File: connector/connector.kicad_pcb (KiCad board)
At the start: 2 copper layers, 18.7 x 4.8 mm, 10 parts, among them P11 CONN_1, P12 CONN_1, P13 CONN_1, P14 CONN_1, P15 CONN_1, P21 CONN_1, P22 CONN_1, P23 CONN_1, P24 CONN_1, P25 CONN_1

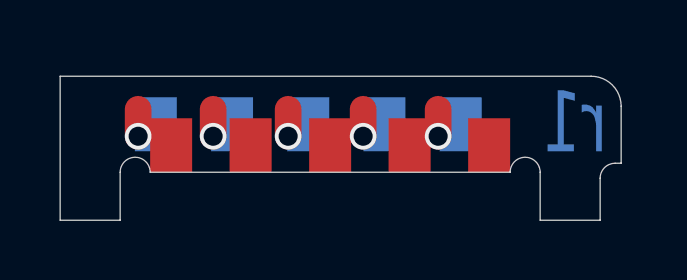
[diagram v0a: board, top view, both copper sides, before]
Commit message: Remove old tracks.
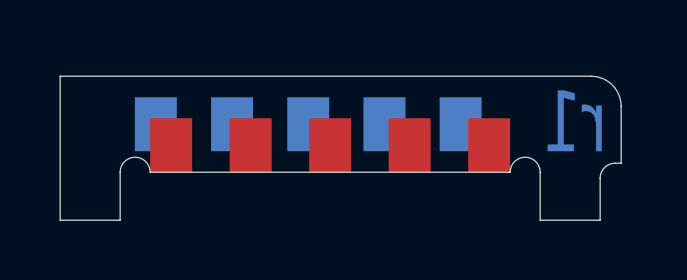
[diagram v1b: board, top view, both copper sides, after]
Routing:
- net N-000005: track 1.82 -> 0.00 mm, vias 1 -> 0
- net N-000004: track 1.78 -> 0.00 mm, vias 1 -> 0
- net N-000003: track 1.74 -> 0.00 mm, vias 1 -> 0
- net N-000002: track 1.70 -> 0.00 mm, vias 1 -> 0
- net N-000001: track 1.66 -> 0.00 mm, vias 1 -> 0
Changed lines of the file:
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@@
   (general
     (links 5)
-    (no_connects 0)
+    (no_connects 5)
     (area 108.257145 78.7 181.149997 104.3542)
     (thickness 1.6002)
     (drawings 21)
-    (tracks 20)
+    (tracks 0)
     (zones 0)
     (modules 10)
@@
   (gr_line (start 138.4 102.4) (end 140.4 102.4) (angle 90) (layer Edge.Cuts) (width 0.01))
   (gr_line (start 140.4 102.4) (end 140.4 100.8) (angle 90) (layer Edge.Cuts) (width 0.01))
-  (via (at 141 99.6) (size 0.889) (drill 0.635) (layers Front Back) (net 1))
-  (segment (start 141 99.6) (end 141.19 99.6) (width 0.889) (layer Back) (net 1))
-  (segment (start 141.19 99.6) (end 141.59 99.2) (width 0.889) (layer Back) (net 1))
-  (segment (start 141 98.7) (end 141 99.6) (width 0.889) (layer Front) (net 1))
-  (via (at 143.5 99.6) (size 0.889) (drill 0.635) (layers Front Back) (net 2))
-  (segment (start 143.5 99.6) (end 143.73 99.6) (width 0.889) (layer Back) (net 2))
-  (segment (start 143.73 99.6) (end 144.13 99.2) (width 0.889) (layer Back) (net 2))
-  (segment (start 143.5 98.7) (end 143.5 99.6) (width 0.889) (layer Front) (net 2))
-  (via (at 146 99.6) (size 0.889) (drill 0.635) (layers Front Back) (net 3))
-  (segment (start 146 99.6) (end 146.27 99.6) (width 0.889) (layer Back) (net 3))
-  (segment (start 146.27 99.6) (end 146.67 99.2) (width 0.889) (layer Back) (net 3))
-  (segment (start 146 98.7) (end 146 99.6) (width 0.889) (layer Front) (net 3))
-  (via (at 148.5 99.6) (size 0.889) (drill 0.635) (layers Front Back) (net 4))
-  (segment (start 148.5 99.6) (end 148.81 99.6) (width 0.889) (layer Back) (net 4))
-  (segment (start 148.81 99.6) (end 149.21 99.2) (width 0.889) (layer Back) (net 4))
-  (segment (start 148.5 98.7) (end 148.5 99.6) (width 0.889) (layer Front) (net 4))
-  (via (at 151 99.6) (size 0.889) (drill 0.635) (layers Front Back) (net 5))
-  (segment (start 151 99.6) (end 151.35 99.6) (width 0.889) (layer Back) (net 5))
-  (segment (start 151.35 99.6) (end 151.75 99.2) (width 0.889) (layer Back) (net 5))
-  (segment (start 151 98.7) (end 151 99.6) (width 0.889) (layer Front) (net 5))
 )

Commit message: Update revision number.
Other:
- board text added: "r2"
- board text removed: "r1"
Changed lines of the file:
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@@
     (arrow2b (pts (xy 138.4 95.6) (xy 139.526504 95.013579)))
   )
-  (gr_text r1 (at 155.5496 99.1616) (layer B.Mask)
+  (gr_text r2 (at 155.5496 99.1616) (layer B.Mask)
     (effects (font (size 2.032 1.524) (thickness 0.3048)) (justify mirror))
   )
-  (gr_text r1 (at 155.5496 99.1616) (layer Back)
+  (gr_text r2 (at 155.5496 99.1616) (layer Back)
     (effects (font (size 2.032 1.524) (thickness 0.3048)) (justify mirror))
   )

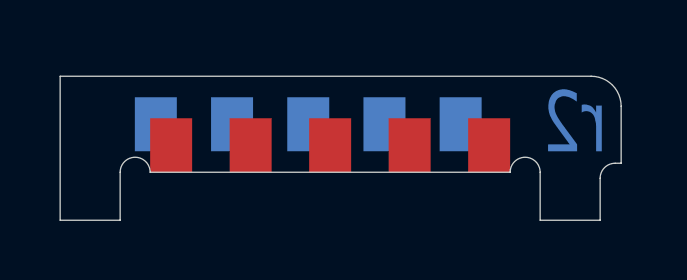
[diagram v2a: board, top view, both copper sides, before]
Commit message: Precisely position vias.
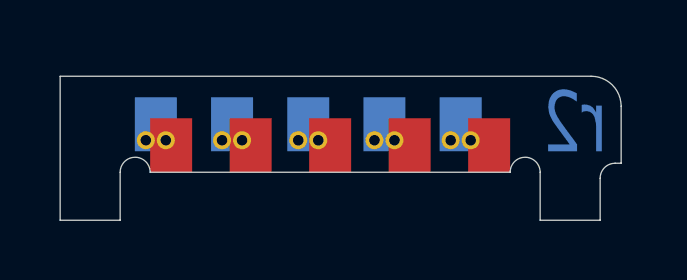
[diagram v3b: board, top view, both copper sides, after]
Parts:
- added ?: VAL**, UGL:via_24_14mil, F.Cu at (141.9, 99.8)
- added via_24_14mil: VAL**, UGL:via_24_14mil, F.Cu at (152.0, 99.7)
- added via_24_14mil: VAL**, UGL:via_24_14mil, F.Cu at (151.4, 99.7)
- added via_24_14mil: VAL**, UGL:via_24_14mil, F.Cu at (148.9, 99.7)
- added via_24_14mil: VAL**, UGL:via_24_14mil, F.Cu at (149.6, 99.7)
- added via_24_14mil: VAL**, UGL:via_24_14mil, F.Cu at (147.0, 99.7)
- added via_24_14mil: VAL**, UGL:via_24_14mil, F.Cu at (146.3, 99.7)
- added via_24_14mil: VAL**, UGL:via_24_14mil, F.Cu at (143.8, 99.7)
- added via_24_14mil: VAL**, UGL:via_24_14mil, F.Cu at (141.3, 99.8)
- added via_24_14mil: VAL**, UGL:via_24_14mil, F.Cu at (144.4, 99.7)
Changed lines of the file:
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@@
 (kicad_pcb (version 4) (host pcbnew "(2014-jul-16 BZR unknown)-product")
   (general
-    (links 5)
-    (no_connects 5)
+    (links 15)
+    (no_connects 0)
     (area 108.257145 78.7 181.149997 104.3542)
     (thickness 1.6002)
@@
     (tracks 0)
     (zones 0)
-    (modules 10)
+    (modules 20)
     (nets 6)
   )
@@
     (mod_text_size 1.524 1.524)
     (mod_text_width 0.3048)
-    (pad_size 1.4 1.8)
-    (pad_drill 0)
+    (pad_size 0.6 0.6)
+    (pad_drill 0.35)
     (pad_to_mask_clearance 0.1016)
     (aux_axis_origin 0 0)
-    (visible_elements FFFFFF7F)
+    (visible_elements FFFFFD7F)
     (pcbplotparams
       (layerselection 0x00030_80000001)
@@
     (add_net N-000005)
   )
+  (module UGL:via_24_14mil (layer Front)
+    (at 152.0444 99.73564)
+    (fp_text reference via_24_14mil (at 0 -1.8) (layer F.SilkS) hide
+      (effects (font (size 1 1) (thickness 0.15)))
+    )
+    (fp_text value VAL** (at 0 1.9) (layer F.SilkS) hide
+      (effects (font (size 1 1) (thickness 0.15)))
+    )
+    (pad "" thru_hole circle (at 0.038933 -0.002307) (size 0.6 0.6) (drill 0.35) (layers *.Cu *.Mask F.SilkS)
+      (net 5 N-000005) (solder_mask_margin -1) (clearance 0.01))
+  )
+  (module UGL:via_24_14mil (layer Front)
+    (at 151.37384 99.73564)
+    (fp_text reference via_24_14mil (at 0 -1.8) (layer F.SilkS) hide
+      (effects (font (size 1 1) (thickness 0.15)))
+    )
+    (fp_text value VAL** (at 0 1.9) (layer F.SilkS) hide
+      (effects (font (size 1 1) (thickness 0.15)))
+    )
+    (pad "" thru_hole circle (at 0.042827 -0.002307) (size 0.6 0.6) (drill 0.35) (layers *.Cu *.Mask F.SilkS)
+      (net 5 N-000005) (solder_mask_margin -1) (clearance 0.01))
+  )
+  (module UGL:via_24_14mil (layer Front)
+    (at 148.87956 99.74072)
+    (fp_text reference via_24_14mil (at 0 -1.8) (layer F.SilkS) hide
+      (effects (font (size 1 1) (thickness 0.15)))
+    )
+    (fp_text value VAL** (at 0 1.9) (layer F.SilkS) hide
+      (effects (font (size 1 1) (thickness 0.15)))
+    )
+    (pad "" thru_hole circle (at -0.002893 -0.007387) (size 0.6 0.6) (drill 0.35) (layers *.Cu *.Mask F.SilkS)
+      (net 4 N-000004) (solder_mask_margin -1) (clearance 0.01))
+  )
+  (module UGL:via_24_14mil (layer Front)
+    (at 149.55012 99.74072)
+    (fp_text reference via_24_14mil (at 0 -1.8) (layer F.SilkS) hide
+      (effects (font (size 1 1) (thickness 0.15)))
+    )
+    (fp_text value VAL** (at 0 1.9) (layer F.SilkS) hide
+      (effects (font (size 1 1) (thickness 0.15)))
+    )
+    (pad "" thru_hole circle (at -0.006787 -0.007387) (size 0.6 0.6) (drill 0.35) (layers *.Cu *.Mask F.SilkS)
+      (net 4 N-000004) (solder_mask_margin -1) (clearance 0.01))
+  )
+  (module UGL:via_24_14mil (layer Front)
+    (at 146.99996 99.7204)
+    (fp_text reference via_24_14mil (at 0 -1.8) (layer F.SilkS) hide
+      (effects (font (size 1 1) (thickness 0.15)))
+    )
+    (fp_text value VAL** (at 0 1.9) (layer F.SilkS) hide
+      (effects (font (size 1 1) (thickness 0.15)))
+    )
+    (pad "" thru_hole circle (at 0.003373 0.012933) (size 0.6 0.6) (drill 0.35) (layers *.Cu *.Mask F.SilkS)
+      (net 3 N-000003) (solder_mask_margin -1) (clearance 0.01))
+  )
+  (module UGL:via_24_14mil (layer Front)
+    (at 146.3294 99.7204)
+    (fp_text reference via_24_14mil (at 0 -1.8) (layer F.SilkS) hide
+      (effects (font (size 1 1) (thickness 0.15)))
+    )
+    (fp_text value VAL** (at 0 1.9) (layer F.SilkS) hide
+      (effects (font (size 1 1) (thickness 0.15)))
+    )
+    (pad "" thru_hole circle (at 0.007267 0.012933) (size 0.6 0.6) (drill 0.35) (layers *.Cu *.Mask F.SilkS)
+      (net 3 N-000003) (solder_mask_margin -1) (clearance 0.01))
+  )
+  (module UGL:via_24_14mil (layer Front)
+    (at 143.77924 99.73564)
+    (fp_text reference via_24_14mil (at 0 -1.8) (layer F.SilkS) hide
+      (effects (font (size 1 1) (thickness 0.15)))
+    )
+    (fp_text value VAL** (at 0 1.9) (layer F.SilkS) hide
+      (effects (font (size 1 1) (thickness 0.15)))
+    )
+    (pad "" thru_hole circle (at 0.017427 -0.002307) (size 0.6 0.6) (drill 0.35) (layers *.Cu *.Mask F.SilkS)
+      (net 2 N-000002) (solder_mask_margin -1) (clearance 0.01))
+  )
   (module vertical_pcb_pad (layer Back)
     (at 151.75 99.2)
@@
       (net 2 N-000002))
   )
+  (module UGL:via_24_14mil (layer Front)
+    (at 141.93012 99.75088)
+    (fp_text reference "" (at 0 -1.8) (layer F.SilkS) hide
+      (effects (font (size 1 1) (thickness 0.15)))
+    )
+    (fp_text value VAL** (at 0 1.9) (layer F.SilkS) hide
+      (effects (font (size 1 1) (thickness 0.15)))
+    )
+    (pad "" thru_hole circle (at -0.006787 -0.017547) (size 0.6 0.6) (drill 0.35) (layers *.Cu *.Mask F.SilkS)
+      (net 1 N-000001) (solder_mask_margin -1) (clearance 0.01))
+  )
+  (module UGL:via_24_14mil (layer Front)
+    (at 141.25956 99.76612)
+    (fp_text reference via_24_14mil (at 0 -1.8) (layer F.SilkS) hide
+      (effects (font (size 1 1) (thickness 0.15)))
+    )
+    (fp_text value VAL** (at 0 1.9) (layer F.SilkS) hide
+      (effects (font (size 1 1) (thickness 0.15)))
+    )
+    (pad "" thru_hole circle (at -0.002893 -0.032787) (size 0.6 0.6) (drill 0.35) (layers *.Cu *.Mask F.SilkS)
+      (net 1 N-000001) (solder_mask_margin -1) (clearance 0.01))
+  )
+  (module UGL:via_24_14mil (layer Front)
+    (at 144.4498 99.73564)
+    (fp_text reference via_24_14mil (at 0 -1.8) (layer F.SilkS) hide
+      (effects (font (size 1 1) (thickness 0.15)))
+    )
+    (fp_text value VAL** (at 0 1.9) (layer F.SilkS) hide
+      (effects (font (size 1 1) (thickness 0.15)))
+    )
+    (pad "" thru_hole circle (at 0.013533 -0.002307) (size 0.6 0.6) (drill 0.35) (layers *.Cu *.Mask F.SilkS)
+      (net 2 N-000002) (solder_mask_margin -1) (clearance 0.01))
+  )
   (gr_text "4.8 mm = 0.188976 in" (at 121.8 100) (layer Cmts.User)

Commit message: Connect the front and back pads.
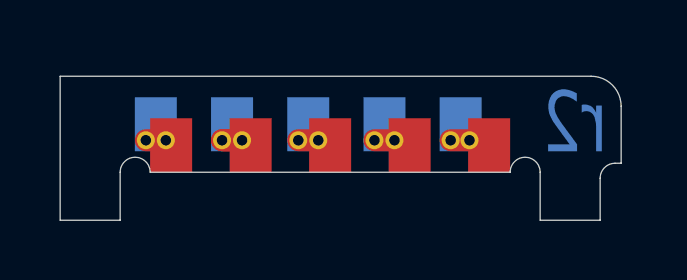
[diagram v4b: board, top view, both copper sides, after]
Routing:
- net N-000002: track 0.00 -> 2.36 mm
- net N-000001: track 0.00 -> 2.23 mm
- net N-000005: track 0.00 -> 2.01 mm
- net N-000004: track 0.00 -> 1.91 mm
- net N-000003: track 0.00 -> 1.80 mm
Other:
- rule trace_min: 0.889 -> 0.6
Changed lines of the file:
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@@
     (thickness 1.6002)
     (drawings 21)
-    (tracks 0)
+    (tracks 22)
     (zones 0)
     (modules 20)
@@
   )
   (setup
-    (last_trace_width 0.889)
-    (user_trace_width 0.889)
+    (last_trace_width 0.733)
+    (user_trace_width 0.733)
     (trace_clearance 0.635)
     (zone_clearance 0.508)
     (zone_45_only no)
-    (trace_min 0.889)
+    (trace_min 0.6)
     (segment_width 0.381)
     (edge_width 0.01016)
@@
     (mod_text_size 1.524 1.524)
     (mod_text_width 0.3048)
-    (pad_size 0.6 0.6)
-    (pad_drill 0.35)
+    (pad_size 1.4 1.8)
+    (pad_drill 0)
     (pad_to_mask_clearance 0.1016)
     (aux_axis_origin 0 0)
-    (visible_elements FFFFFD7F)
+    (visible_elements FFFFFF7F)
     (pcbplotparams
       (layerselection 0x00030_80000001)
@@
       (effects (font (size 1 1) (thickness 0.15)))
     )
-    (pad "" thru_hole circle (at 0.038933 -0.002307) (size 0.6 0.6) (drill 0.35) (layers *.Cu *.Mask F.SilkS)
+    (pad "" thru_hole circle (at 0 -0.002307) (size 0.6 0.6) (drill 0.35) (layers *.Cu *.Mask F.SilkS)
       (net 5 N-000005) (solder_mask_margin -1) (clearance 0.01))
   )
@@
   (gr_line (start 138.4 102.4) (end 140.4 102.4) (angle 90) (layer Edge.Cuts) (width 0.01))
   (gr_line (start 140.4 102.4) (end 140.4 100.8) (angle 90) (layer Edge.Cuts) (width 0.01))
+  (segment (start 141.93012 99.74072) (end 141.59 99.2) (width 0.733) (layer Back) (net 1))
+  (segment (start 141.59 99.2) (end 141.93012 99.54012) (width 0.733) (layer Back) (net 1))
+  (segment (start 141.93012 99.54012) (end 141.93012 99.74072) (width 0.733) (layer Back) (net 1))
+  (segment (start 141.256667 99.733333) (end 141.933333 99.733333) (width 0.733) (layer Front) (net 1))
+  (segment (start 141.933333 99.733333) (end 142.1 99.9) (width 0.733) (layer Front) (net 1))
+  (segment (start 144.13 99.2) (end 144.13 99.4) (width 0.733) (layer Back) (net 2))
+  (segment (start 144.583333 99.733333) (end 143.796667 99.733333) (width 0.733) (layer Front) (net 2))
+  (segment (start 144.75 99.9) (end 144.583333 99.733333) (width 0.733) (layer Front) (net 2))
+  (segment (start 144.13 99.4) (end 143.796667 99.733333) (width 0.733) (layer Back) (net 2))
+  (segment (start 143.796667 99.733333) (end 144.463333 99.733333) (width 0.733) (layer Front) (net 2))
+  (segment (start 146.67 99.2) (end 147.003333 99.533333) (width 0.733) (layer Back) (net 3))
+  (segment (start 147.003333 99.533333) (end 147.003333 99.733333) (width 0.733) (layer Back) (net 3))
+  (segment (start 147.4 99.9) (end 147.233333 99.733333) (width 0.733) (layer Front) (net 3))
+  (segment (start 147.233333 99.733333) (end 146.336667 99.733333) (width 0.733) (layer Front) (net 3))
+  (segment (start 149.21 99.2) (end 149.543333 99.533333) (width 0.733) (layer Back) (net 4))
+  (segment (start 149.543333 99.533333) (end 149.543333 99.733333) (width 0.733) (layer Back) (net 4))
+  (segment (start 150.05 99.9) (end 149.883333 99.733333) (width 0.733) (layer Front) (net 4))
+  (segment (start 149.883333 99.733333) (end 148.876667 99.733333) (width 0.733) (layer Front) (net 4))
+  (segment (start 151.75 99.2) (end 152.0444 99.4944) (width 0.733) (layer Back) (net 5))
+  (segment (start 152.0444 99.4944) (end 152.0444 99.733333) (width 0.733) (layer Back) (net 5))
+  (segment (start 152.7 99.9) (end 152.533333 99.733333) (width 0.733) (layer Front) (net 5))
+  (segment (start 152.533333 99.733333) (end 151.416667 99.733333) (width 0.733) (layer Front) (net 5))
 )
